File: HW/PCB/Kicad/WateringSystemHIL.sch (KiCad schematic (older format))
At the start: 50 parts, among them J1 USB_B_Micro_VBUS_Input, J13 USB_B_Micro, J16 Boot_H, J17 Boot_L, J18 Encoder_PINA, J19 Encoder_PINB, J20 Encoder_SW, J3 Raspberry Pi Zero WH, J4 MEAS_VIN, J5 MEAS_I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

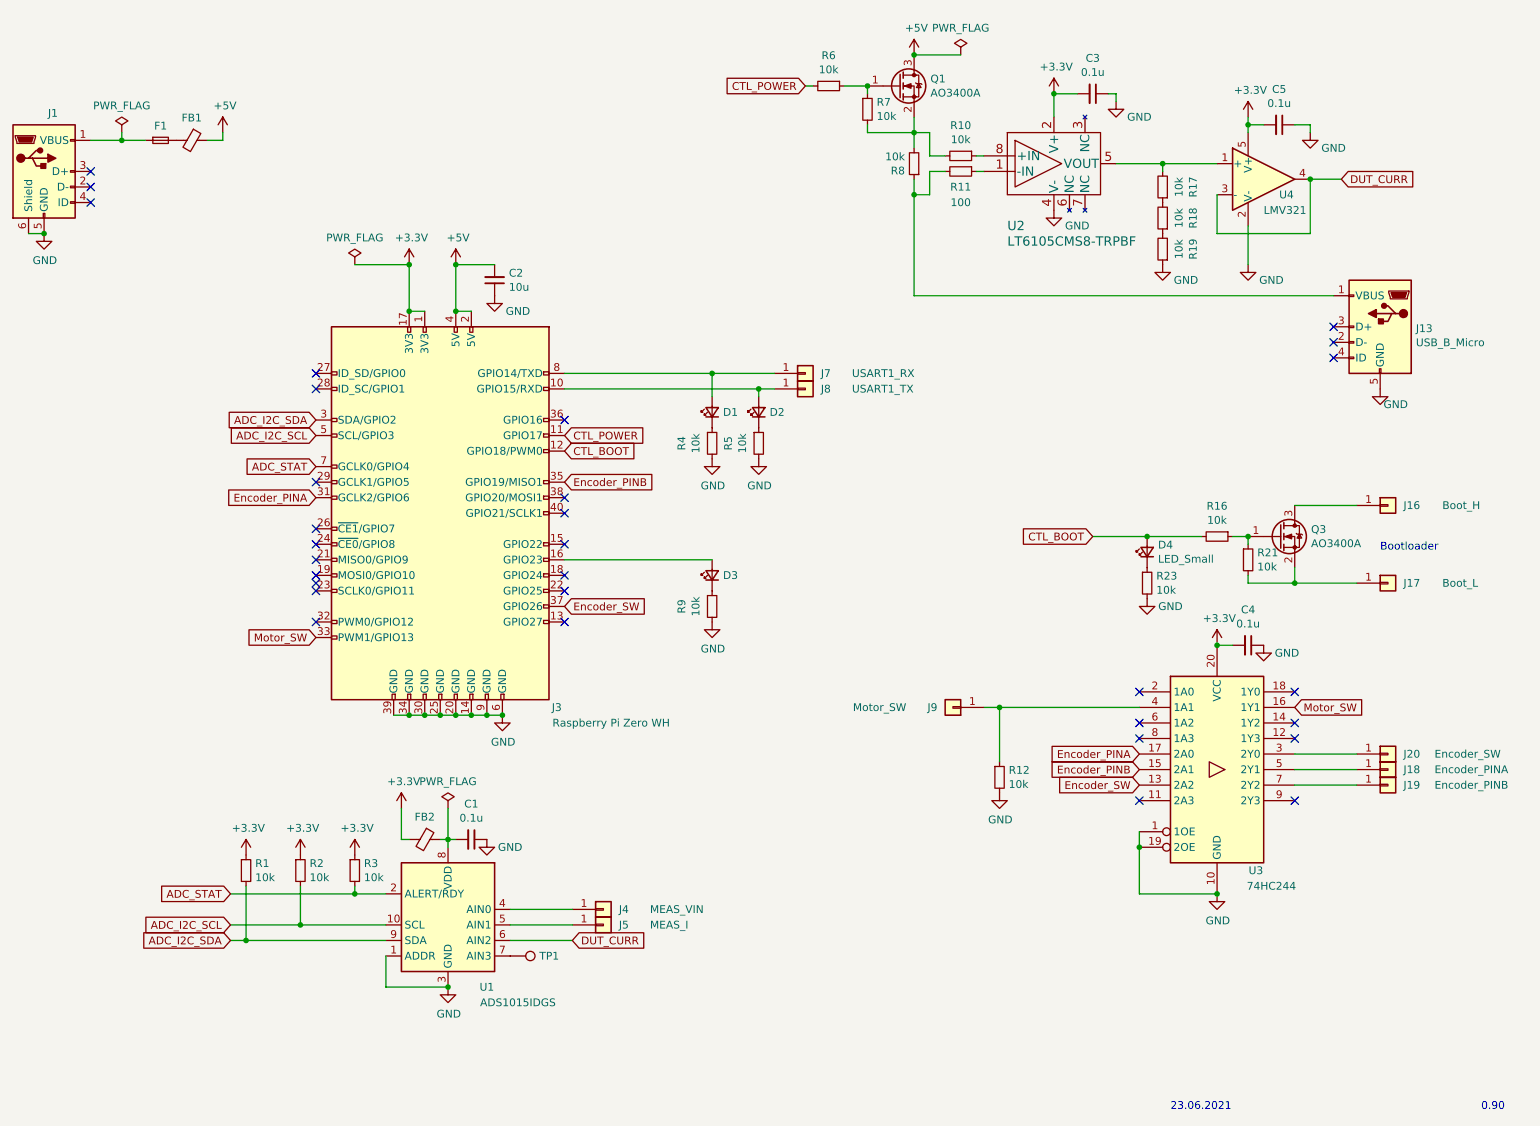
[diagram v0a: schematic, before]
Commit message: PCB v0.9.1
Added
- Status LEDs for Power, DUT Power, Linked

Changed
- Active signal state of DUT->TS LED and TS->DUT LED. Turn ON the LEDs when the signals are Low level.

Fixed
- An issue where the micro USB plug could not be mounted on the PCB properlly. The micro USB plub was replaced with GCT USB3150.
- An issue where boot mode of WateringSystem was not properlly controlled. Use 74HC244 to control Boot_L signal.
- An issue where power switch of WateringSystem was not properlly controlled. Use a P-Channel MOSFET(AO3401) instead of N-Channel MOSFET(AO3400).
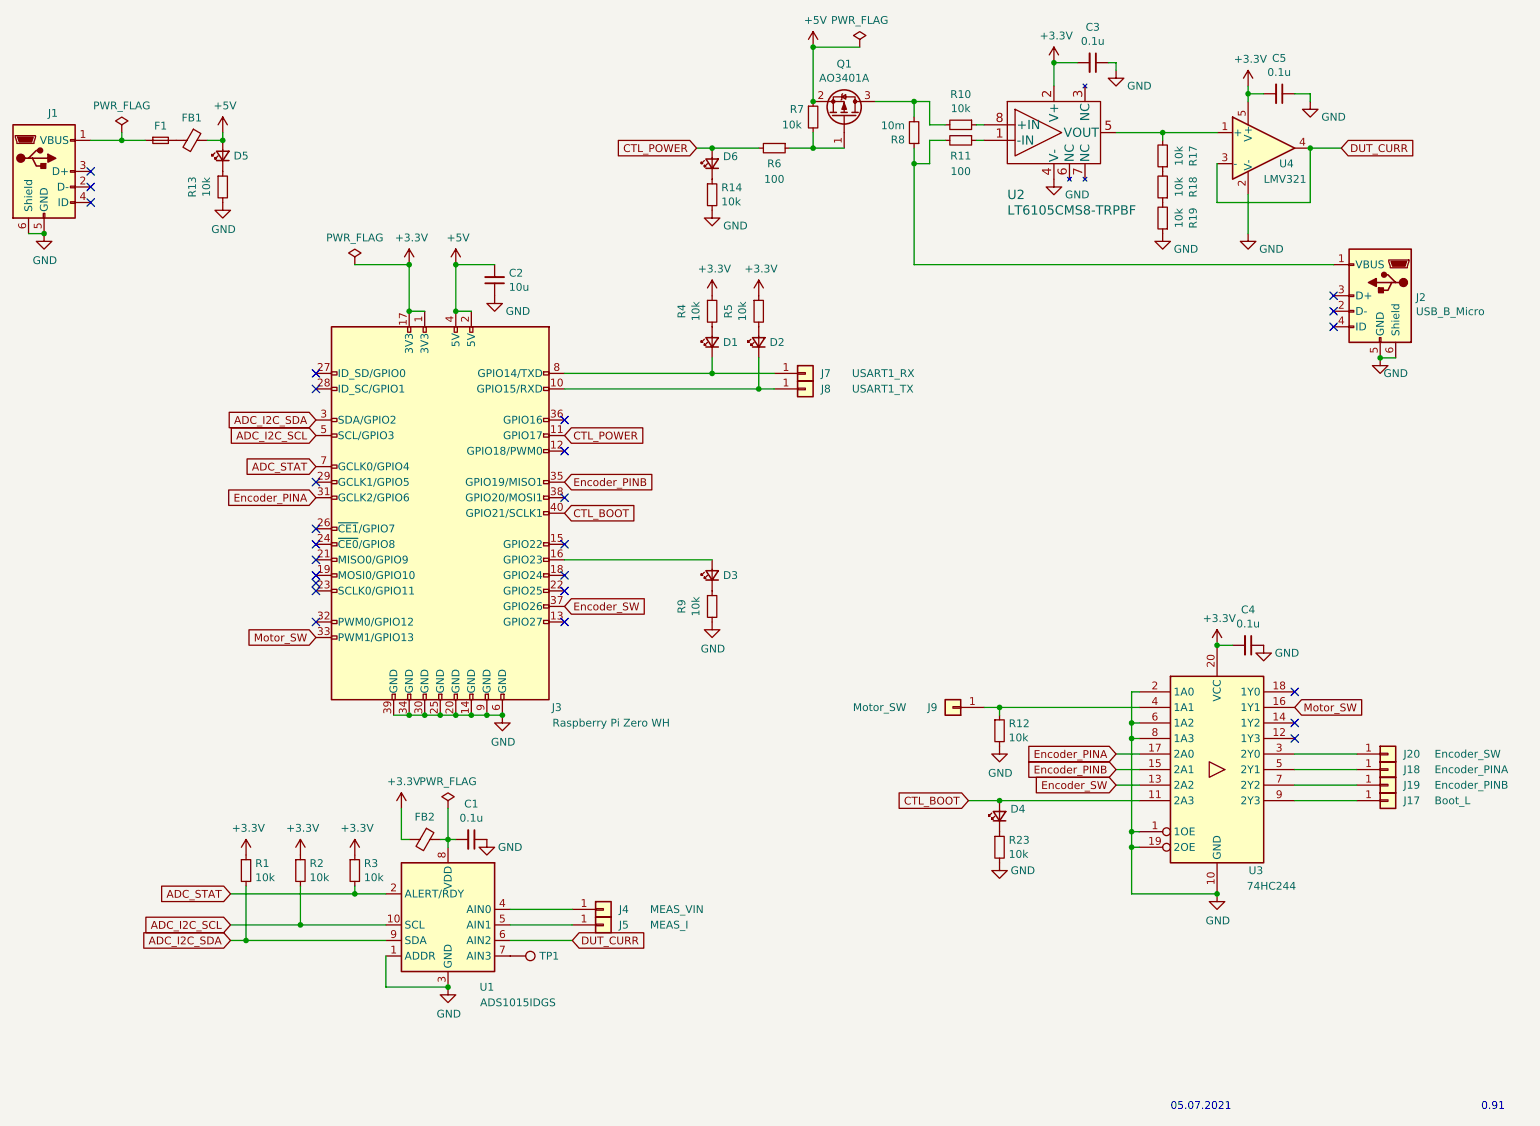
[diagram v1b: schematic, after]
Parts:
- removed J13: USB_B_Micro, WateringSystemHIL:BKL_MicroUSBPlug_10120262, symbol WateringSystemHIL:USB_B_Micro_VBUS_Output_No_Shield
- removed J16: Boot_H, WateringSystemHIL:P100-E2 Pogo Spring Test Probe Pin, symbol Connector_Generic:Conn_01x01
- removed Q1, Q3: AO3400A, Package_TO_SOT_SMD:SOT-23, symbol Transistor_FET:AO3400A
- removed R16, R21: 10k, Capacitor_SMD:C_0805_2012Metric_Pad1.18x1.45mm_HandSolder, symbol Device:R_Small
- added D5, D6: LED_Small, LED_SMD:LED_0603_1608Metric_Pad1.05x0.95mm_HandSolder, symbol Device:LED_Small
- added J2: USB_B_Micro, WateringSystemHIL:GCT_USB3150-30-130-A, symbol Connector:USB_B_Micro
- added Q1: AO3401A, Package_TO_SOT_SMD:SOT-23_Handsoldering, symbol Transistor_FET:AO3401A
- added R13, R14: 10k, Capacitor_SMD:C_0805_2012Metric_Pad1.18x1.45mm_HandSolder, symbol Device:R_Small
- R6: value 10k -> 100
- R8: value 10k -> 10m
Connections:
- net +3V3: now also R4.1, R5.1
- net +5V: now also R7.1, D5.2 (A), Q1.2 (S)
- net CTL_BOOT: now also J3.40 (GPIO21/SCLK1), U3.11 (2A3); no longer J3.12 (GPIO18/PWM0)
- net CTL_POWER: now also D6.2 (A)
- net GND: now also U3.2 (1A0), U3.6 (1A2), U3.8 (1A3), J2.5 (GND), J2.6 (Shield), R13.2, R14.2; no longer R4.2, R5.2
- net at J3.10 (GPIO15/RXD), J8.1 (Pin_1): now also D2.1 (K); no longer D2.2 (A)
- net at J3.8 (GPIO14/TXD), J7.1 (Pin_1): now also D1.1 (K); no longer D1.2 (A)
- net at R10.2, R8.2: now also Q1.3 (D); no longer R7.2
- net at R11.2, R8.1: now also J2.1 (VBUS)
- net at J17.1 (Pin_1): now also U3.9 (2Y3)
- net at R6.1: now also R7.2, Q1.1 (G); no longer R7.1
- new net: D5.1 (K), R13.1
- new net: D6.1 (K), R14.1
- new net: D1.2 (A), R4.2
- new net: D2.2 (A), R5.2
- no-connect marks 31 -> 26
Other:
- note added: "0.91"
- note added: "05.07.2021"
- note removed: "0.90"
- note removed: "23.06.2021"
- note removed: "Bootloader"
- moved on the sheet: C3, C5, D1, D2, D4, J17, R10, R11, R12, R17, R18, R19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

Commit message: Fixed wrong connection of Encoder_SW, Encoder_PINA and Encoder_PINB at 74HC244. Changed polarity of USART1_RX and USART1_TX status LEDs in order for the LEDs to light when data is transmitted. Removed an unity gain buffer (U4, LMV321) because it causes unignorable offset voltage (around 10mV) as it is used with a single power supply. Changed to use a high side switch (AP2151) instead of MOSFET (AO3401) to control power supply for the DUT.
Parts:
- removed C5: 0.1u, Capacitor_SMD:C_0805_2012Metric_Pad1.18x1.45mm_HandSolder, symbol Device:C_Small
- removed Q1: AO3401A, Package_TO_SOT_SMD:SOT-23_Handsoldering, symbol Transistor_FET:AO3401A
- removed R6: 100, Capacitor_SMD:C_0805_2012Metric_Pad1.18x1.45mm_HandSolder, symbol Device:R_Small
- removed R7: 10k, Capacitor_SMD:C_0805_2012Metric_Pad1.18x1.45mm_HandSolder, symbol Device:R_Small
- removed U4: LMV321, Package_TO_SOT_SMD:SOT-23-5_HandSoldering, symbol Amplifier_Operational:LMV321
- added U5: AP2151W, Package_TO_SOT_SMD:SOT-23-5, symbol Power_Management:AP2171W
- R10: value 10k -> 100
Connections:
- wire segments 108 -> 95
- no-connect marks 26 -> 27
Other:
- note added: "1.00"
- note added: "21.08.2021"
- note removed: "0.91"
- note removed: "05.07.2021"
- moved on the sheet: D6, R14
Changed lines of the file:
@@
 L power:+5V #PWR019
 U 1 1 60D6EF62
-P 6450 800
-F 0 "#PWR019" H 6450 650 50  0001 C CNN
-F 1 "+5V" H 6465 973 50  0000 C CNN
-F 2 "" H 6450 800 50  0001 C CNN
-F 3 "" H 6450 800 50  0001 C CNN
-	1    6450 800
+P 5750 1000
+F 0 "#PWR019" H 5750 850 50  0001 C CNN
+F 1 "+5V" H 5765 1173 50  0000 C CNN
+F 2 "" H 5750 1000 50  0001 C CNN
+F 3 "" H 5750 1000 50  0001 C CNN
+	1    5750 1000
 	1    0    0    -1
 $EndComp
@@
 $EndComp
 $Comp
-L Device:R_Small R7
-U 1 1 60DBDBF7
-P 6450 1250
-F 0 "R7" H 6300 1300 50  0000 L CNN
-F 1 "10k" H 6250 1200 50  0000 L CNN
-F 2 "Capacitor_SMD:C_0805_2012Metric_Pad1.18x1.45mm_HandSolder" H 6450 1250 50  0001 C CNN
-F 3 "~" H 6450 1250 50  0001 C CNN
-	1    6450 1250
-	1    0    0    -1
-$EndComp
-$Comp
-L Device:R_Small R6
-U 1 1 60DD1C97
-P 6200 1450
-F 0 "R6" V 6300 1450 50  0000 C CNN
-F 1 "100" V 6400 1450 50  0000 C CNN
-F 2 "Capacitor_SMD:C_0805_2012Metric_Pad1.18x1.45mm_HandSolder" H 6200 1450 50  0001 C CNN
-F 3 "~" H 6200 1450 50  0001 C CNN
-	1    6200 1450
-	0    1    1    0
-$EndComp
-$Comp
 L Device:Ferrite_Bead_Small FB2
 U 1 1 60DE6AB0
@@
 P 7400 1300
 F 0 "R10" V 7204 1300 50  0000 C CNN
-F 1 "10k" V 7295 1300 50  0000 C CNN
+F 1 "100" V 7295 1300 50  0000 C CNN
 F 2 "Capacitor_SMD:C_0805_2012Metric_Pad1.18x1.45mm_HandSolder" H 7400 1300 50  0001 C CNN
 F 3 "~" H 7400 1300 50  0001 C CNN
@@
 	7500 1400 7550 1400
 $Comp
-L Amplifier_Operational:LMV321 U4
-U 1 1 60CEC5D1
-P 9350 1450
-F 0 "U4" H 9450 1350 50  0000 L CNN
-F 1 "LMV321" H 9350 1250 50  0000 L CNN
-F 2 "Package_TO_SOT_SMD:SOT-23-5_HandSoldering" H 9350 1450 50  0001 L CNN
-F 3 "http://www.ti.com/lit/ds/symlink/lmv324.pdf" H 9350 1450 50  0001 C CNN
-	1    9350 1450
-	1    0    0    -1
-$EndComp
-$Comp
 L Device:R_Small R8
 U 1 1 60D30F7A
@@
 	-1   0    0    1
 $EndComp
-Text GLabel 5700 1450 0    50   Input ~ 0
+Text GLabel 5700 1350 0    50   Input ~ 0
 CTL_POWER
 Text GLabel 7450 5650 0    50   Input ~ 0
 CTL_BOOT
 Wire Wire Line
-	5700 1450 5800 1450
+	5700 1350 5800 1350
 Text GLabel 4850 3300 2    50   Input ~ 0
 CTL_POWER
@@
 Text GLabel 4850 4400 2    50   Input ~ 0
 Encoder_SW
+Text GLabel 8400 5450 0    50   Input ~ 0
+Encoder_PINA
+Text GLabel 8400 5550 0    50   Input ~ 0
+Encoder_PINB
 Text GLabel 8400 5350 0    50   Input ~ 0
-Encoder_PINA
-Text GLabel 8400 5450 0    50   Input ~ 0
-Encoder_PINB
-Text GLabel 8400 5550 0    50   Input ~ 0
 Encoder_SW
 Text GLabel 3250 4600 0    50   Input ~ 0
@@
 Wire Wire Line
 	8700 1350 8700 1400
-$Comp
-L power:GND #PWR031
-U 1 1 60E7365F
-P 9250 2000
-F 0 "#PWR031" H 9250 1750 50  0001 C CNN
-F 1 "GND" H 9400 1900 50  0000 C CNN
-F 2 "" H 9250 2000 50  0001 C CNN
-F 3 "" H 9250 2000 50  0001 C CNN
-	1    9250 2000
-	1    0    0    -1
-$EndComp
-Wire Wire Line
-	9250 1750 9250 2000
-Wire Wire Line
-	9050 1550 9050 1800
-Wire Wire Line
-	9050 1800 9650 1800
-Wire Wire Line
-	9650 1800 9650 1450
-$Comp
-L Device:C_Small C5
-U 1 1 60E7A1C3
-P 9450 1100
-F 0 "C5" V 9221 1100 50  0000 C CNN
-F 1 "0.1u" V 9312 1100 50  0000 C CNN
-F 2 "Capacitor_SMD:C_0805_2012Metric_Pad1.18x1.45mm_HandSolder" H 9450 1100 50  0001 C CNN
-F 3 "~" H 9450 1100 50  0001 C CNN
-	1    9450 1100
-	0    1    1    0
-$EndComp
-$Comp
-L power:GND #PWR033
-U 1 1 60E7B7BA
-P 9650 1150
-F 0 "#PWR033" H 9650 900 50  0001 C CNN
-F 1 "GND" H 9800 1050 50  0000 C CNN
-F 2 "" H 9650 1150 50  0001 C CNN
-F 3 "" H 9650 1150 50  0001 C CNN
-	1    9650 1150
-	1    0    0    -1
-$EndComp
-Wire Wire Line
-	9250 1150 9250 1100
-Wire Wire Line
-	9350 1100 9250 1100
-Connection ~ 9250 1100
-Wire Wire Line
-	9250 1100 9250 1050
-Wire Wire Line
-	9550 1100 9650 1100
-Wire Wire Line
-	9650 1100 9650 1150
 Wire Wire Line
 	8700 1350 9050 1350
@@
 Text GLabel 4900 6550 2    50   Input ~ 0
 DUT_CURR
-Text GLabel 9850 1450 2    50   Input ~ 0
+Text GLabel 9050 1350 2    50   Input ~ 0
 DUT_CURR
-Wire Wire Line
-	9850 1450 9650 1450
-Connection ~ 9650 1450
 Wire Wire Line
 	7100 1150 7100 1250
@@
 $EndComp
 Text Notes 8750 7650 0    50   ~ 0
-05.07.2021
+21.08.2021
 Text Notes 10750 7650 0    50   ~ 0
-0.91
+1.00
 $Comp
 L Device:LED_Small D4
@@
 	1    0    0    -1
 $EndComp
-$Comp
-L power:+3.3V #PWR030
-U 1 1 6111C955
-P 9250 1050
-F 0 "#PWR030" H 9250 900 50  0001 C CNN
-F 1 "+3.3V" H 9265 1223 50  0000 C CNN
-F 2 "" H 9250 1050 50  0001 C CNN
-F 3 "" H 9250 1050 50  0001 C CNN
-	1    9250 1050
-	1    0    0    -1
-$EndComp
 Wire Wire Line
 	2000 1400 2150 1400
@@
 L power:PWR_FLAG #FLG04
 U 1 1 61124723
-P 6750 800
-F 0 "#FLG04" H 6750 875 50  0001 C CNN
-F 1 "PWR_FLAG" H 6750 973 50  0000 C CNN
-F 2 "" H 6750 800 50  0001 C CNN
-F 3 "~" H 6750 800 50  0001 C CNN
-	1    6750 800
-	1    0    0    -1
-$EndComp
-Wire Wire Line
-	6750 800  6450 800
+P 6050 1000
+F 0 "#FLG04" H 6050 1075 50  0001 C CNN
+F 1 "PWR_FLAG" H 6050 1173 50  0000 C CNN
+F 2 "" H 6050 1000 50  0001 C CNN
+F 3 "~" H 6050 1000 50  0001 C CNN
+	1    6050 1000
+	1    0    0    -1
+$EndComp
+Wire Wire Line
+	6050 1000 5750 1000
 $Comp
 L power:GND #PWR034
@@
 Wire Wire Line
 	9550 5650 9950 5650
-$Comp
-L Transistor_FET:AO3401A Q1
-U 1 1 60E5B505
-P 6650 1250
-F 0 "Q1" V 6992 1250 50  0000 C CNN
-F 1 "AO3401A" V 6901 1250 50  0000 C CNN
-F 2 "Package_TO_SOT_SMD:SOT-23_Handsoldering" H 6850 1175 50  0001 L CIN
-F 3 "http://www.aosmd.com/pdfs/datasheet/AO3401A.pdf" H 6650 1250 50  0001 L CNN
-	1    6650 1250
-	0    1    -1   0
-$EndComp
-Wire Wire Line
-	6300 1450 6450 1450
-Wire Wire Line
-	6450 1350 6450 1450
-Connection ~ 6450 1450
-Wire Wire Line
-	6450 1450 6650 1450
-Wire Wire Line
-	6450 800  6450 1150
-Connection ~ 6450 800
-Connection ~ 6450 1150
 Wire Wire Line
 	6850 1150 7100 1150
@@
 L Device:LED_Small D6
 U 1 1 60E9DFB6
-P 5800 1550
-F 0 "D6" V 5846 1480 50  0000 R CNN
-F 1 "LED_Small" V 5755 1480 50  0001 R CNN
-F 2 "LED_SMD:LED_0603_1608Metric_Pad1.05x0.95mm_HandSolder" V 5800 1550 50  0001 C CNN
-F 3 "~" V 5800 1550 50  0001 C CNN
-	1    5800 1550
+P 5800 1450
+F 0 "D6" V 5846 1380 50  0000 R CNN
+F 1 "LED_Small" V 5755 1380 50  0001 R CNN
+F 2 "LED_SMD:LED_0603_1608Metric_Pad1.05x0.95mm_HandSolder" V 5800 1450 50  0001 C CNN
+F 3 "~" V 5800 1450 50  0001 C CNN
+	1    5800 1450
 	0    -1   -1   0
 $EndComp
-Connection ~ 5800 1450
-Wire Wire Line
-	5800 1450 6100 1450
+Connection ~ 5800 1350
+Wire Wire Line
+	5800 1350 6050 1350
 $Comp
 L Device:R_Small R14
 U 1 1 60EA1998
-P 5800 1750
-F 0 "R14" H 5859 1796 50  0000 L CNN
-F 1 "10k" H 5859 1705 50  0000 L CNN
-F 2 "Capacitor_SMD:C_0805_2012Metric_Pad1.18x1.45mm_HandSolder" H 5800 1750 50  0001 C CNN
-F 3 "~" H 5800 1750 50  0001 C CNN
-	1    5800 1750
+P 5800 1650
+F 0 "R14" H 5859 1696 50  0000 L CNN
+F 1 "10k" H 5859 1605 50  0000 L CNN
+F 2 "Capacitor_SMD:C_0805_2012Metric_Pad1.18x1.45mm_HandSolder" H 5800 1650 50  0001 C CNN
+F 3 "~" H 5800 1650 50  0001 C CNN
+	1    5800 1650
 	1    0    0    -1
 $EndComp
@@
 L power:GND #PWR04
 U 1 1 60EA1D7B
-P 5800 1850
-F 0 "#PWR04" H 5800 1600 50  0001 C CNN
-F 1 "GND" H 5950 1750 50  0000 C CNN
-F 2 "" H 5800 1850 50  0001 C CNN
-F 3 "" H 5800 1850 50  0001 C CNN
-	1    5800 1850
-	1    0    0    -1
-$EndComp
-Wire Wire Line
-	8550 5350 8400 5350
-Wire Wire Line
-	8550 5450 8400 5450
-Wire Wire Line
-	8550 5550 8400 5550
+P 5800 1750
+F 0 "#PWR04" H 5800 1500 50  0001 C CNN
+F 1 "GND" H 5950 1650 50  0000 C CNN
+F 2 "" H 5800 1750 50  0001 C CNN
+F 3 "" H 5800 1750 50  0001 C CNN
+	1    5800 1750
+	1    0    0    -1
+$EndComp
 Wire Wire Line
 	8550 4950 8500 4950
@@
 	10200 2800 10100 2800
 Connection ~ 10100 2800
+$Comp
+L Power_Management:AP2171W U5
+U 1 1 60FEB9B3
+P 6450 1250
+F 0 "U5" H 6450 1617 50  0000 C CNN
+F 1 "AP2151W" H 6450 1526 50  0000 C CNN
+F 2 "Package_TO_SOT_SMD:SOT-23-5" H 6450 850 50  0001 C CNN
+F 3 "https://www.diodes.com/assets/Datasheets/AP2161.pdf" H 6450 1300 50  0001 C CNN
+	1    6450 1250
+	1    0    0    -1
+$EndComp
+Connection ~ 6050 1000
+Wire Wire Line
+	6050 1000 6050 1150
+NoConn ~ 6850 1350
+$Comp
+L power:GND #PWR018
+U 1 1 61005299
+P 6450 1550
+F 0 "#PWR018" H 6450 1300 50  0001 C CNN
+F 1 "GND" H 6600 1450 50  0000 C CNN
+F 2 "" H 6450 1550 50  0001 C CNN
+F 3 "" H 6450 1550 50  0001 C CNN
+	1    6450 1550
+	1    0    0    -1
+$EndComp
+Wire Wire Line
+	8400 5350 8550 5350
+Wire Wire Line
+	8400 5450 8550 5450
+Wire Wire Line
+	8400 5550 8550 5550
 $EndSCHEMATC

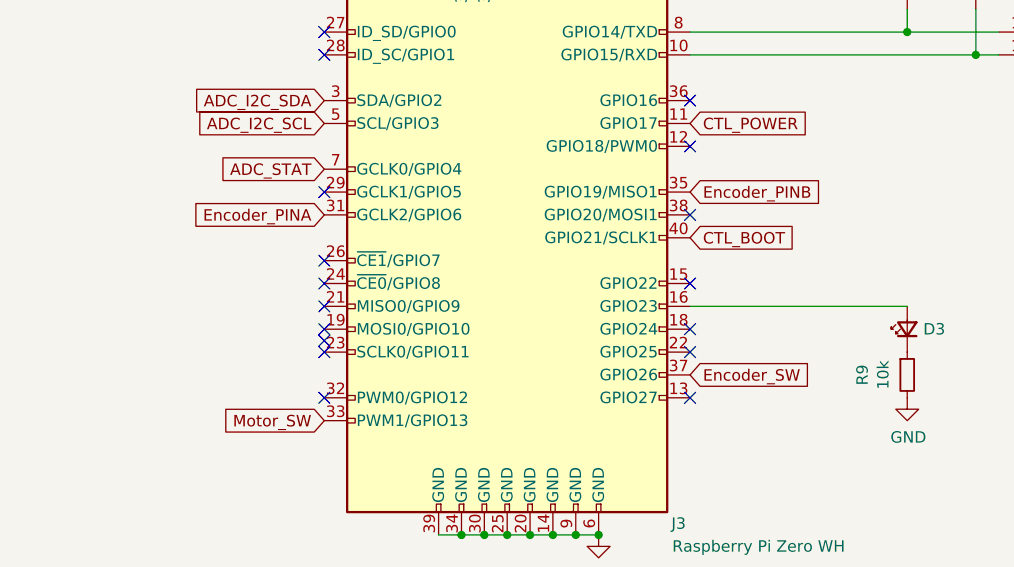
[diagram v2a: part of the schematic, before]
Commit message: Changed to use a pin socket instead of a pin header for a connector for the Raspberry Pi.
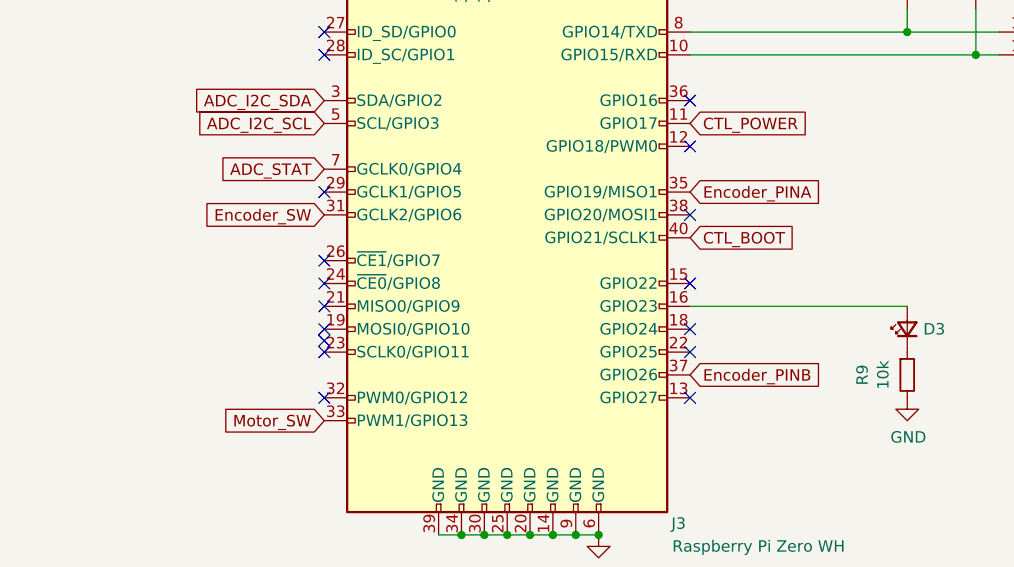
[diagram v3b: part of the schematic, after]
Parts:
- J3: footprint Connector_PinHeader_2.54mm:PinHeader_2x20_P2.54mm_Vertical -> Connector_PinSocket_2.54mm:PinSocket_2x20_P2.54mm_Vertical
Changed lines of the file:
@@
 F 0 "J3" H 3300 2550 50  0000 C CNN
 F 1 "Raspberry Pi Zero WH" H 2950 2450 50  0000 C CNN
-F 2 "Connector_PinHeader_2.54mm:PinHeader_2x20_P2.54mm_Vertical" H 4050 3800 50  0001 C CNN
+F 2 "Connector_PinSocket_2.54mm:PinSocket_2x20_P2.54mm_Vertical" H 4050 3800 50  0001 C CNN
 F 3 "https://www.raspberrypi.org/documentation/hardware/raspberrypi/schematics/rpi_SCH_3bplus_1p0_reduced.pdf" H 4050 3800 50  0001 C CNN
 	1    4050 3800
@@
 	2700 6550 2800 6550
 Connection ~ 2800 6550
+Text GLabel 4850 3600 2    50   Input ~ 0
+Encoder_PINA
+Text GLabel 4850 4400 2    50   Input ~ 0
+Encoder_PINB
 Text GLabel 3250 3700 0    50   Input ~ 0
-Encoder_PINA
-Text GLabel 4850 3600 2    50   Input ~ 0
-Encoder_PINB
-Text GLabel 4850 4400 2    50   Input ~ 0
 Encoder_SW
 Text GLabel 8400 5450 0    50   Input ~ 0
